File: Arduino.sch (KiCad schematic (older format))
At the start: 18 parts

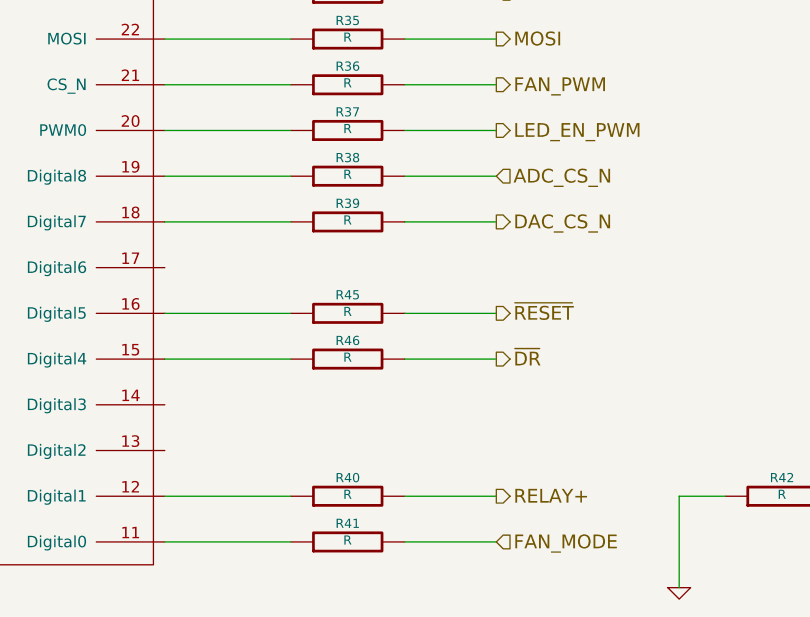
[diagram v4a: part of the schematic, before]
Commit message: Associated and placed the Current/Fan Driver Module
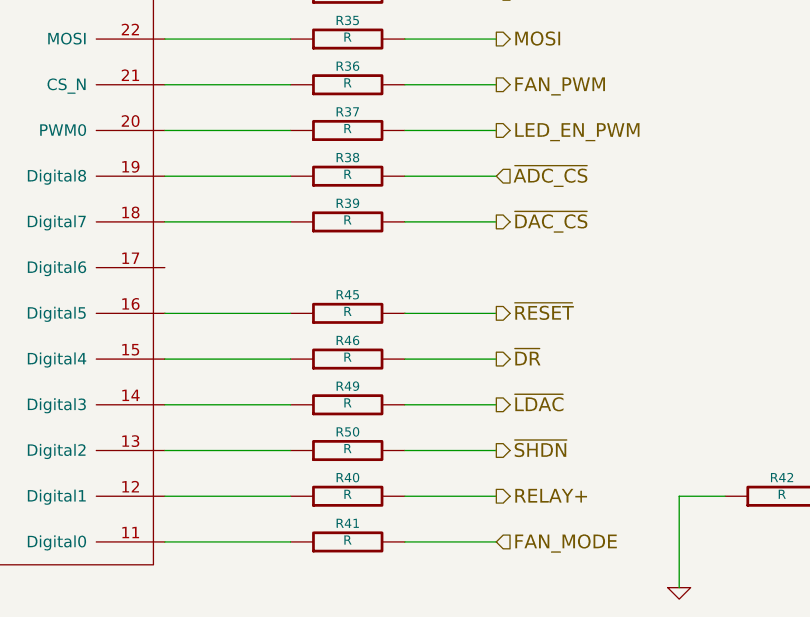
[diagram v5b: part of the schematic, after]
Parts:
- added R49, R50: R, symbol R
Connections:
- net at ARD1.13 (Digital2): now also R50.1
- net at ARD1.14 (Digital3): now also R49.1
- net ADC_CS_N renamed ~ADC_CS
- net DAC_CS_N renamed ~DAC_CS
- new net ~LDAC: R49.2
- new net ~SHDN: R50.2
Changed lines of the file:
@@
 SCLK
 Text HLabel 7100 4000 2    60   Output ~ 0
-DAC_CS_N
+~DAC_CS
 Text HLabel 7100 3400 2    60   Output ~ 0
 FAN_PWM
@@
 	7900 5200 7900 5600
 $Comp
-L GND #PWR61
+L GND #PWR65
 U 1 1 52FC2D3A
 P 7900 5600
-F 0 "#PWR61" H 7900 5600 30  0001 C CNN
+F 0 "#PWR65" H 7900 5600 30  0001 C CNN
 F 1 "GND" H 7900 5530 30  0001 C CNN
 F 2 "" H 7900 5600 60  0000 C CNN
@@
 	5650 3600 6200 3600
 Text HLabel 7100 3800 2    60   Input ~ 0
-ADC_CS_N
+~ADC_CS
 $Comp
 L R R38
@@
 	3200 4000 3750 4000
 $Comp
-L +12P #PWR60
+L +12P #PWR64
 U 1 1 52FC23FA
 P 2300 3800
-F 0 "#PWR60" H 2300 3770 30  0001 C CNN
+F 0 "#PWR64" H 2300 3770 30  0001 C CNN
 F 1 "+12P" H 2300 3900 30  0000 C CNN
 F 2 "" H 2300 3800 60  0000 C CNN
@@
 Wire Wire Line
 	5650 4600 6200 4600
+Text HLabel 7100 4800 2    60   Output ~ 0
+~LDAC
+$Comp
+L R R49
+U 1 1 53090D0D
+P 6450 4800
+F 0 "R49" V 6530 4800 40  0000 C CNN
+F 1 "R" V 6457 4801 40  0000 C CNN
+F 2 "" V 6380 4800 30  0000 C CNN
+F 3 "" H 6450 4800 30  0000 C CNN
+	1    6450 4800
+	0    -1   -1   0
+$EndComp
+Wire Wire Line
+	6700 4800 7100 4800
+Wire Wire Line
+	5650 4800 6200 4800
+Text HLabel 7100 5000 2    60   Output ~ 0
+~SHDN
+$Comp
+L R R50
+U 1 1 53090D16
+P 6450 5000
+F 0 "R50" V 6530 5000 40  0000 C CNN
+F 1 "R" V 6457 5001 40  0000 C CNN
+F 2 "" V 6380 5000 30  0000 C CNN
+F 3 "" H 6450 5000 30  0000 C CNN
+	1    6450 5000
+	0    -1   -1   0
+$EndComp
+Wire Wire Line
+	6700 5000 7100 5000
+Wire Wire Line
+	5650 5000 6200 5000
 $EndSCHEMATC
